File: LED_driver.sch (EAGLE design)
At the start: 15 parts

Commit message: Almost done with version 1 of the LED Driver Board
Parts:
- removed C4: 4.7uF 80V, resistor:C-EUC1210
- removed C6: 10uF, resistor:C-EUC0603
- removed U$11: VREG-ZXTR2105, BlueRobotics-Main:VREG-ZXTR2105
- removed U$3: 10uH, BlueRobotics-Main:INDUCTOR8040
- added C8: 47uF, PowerComponents:C-TANTALUM(10UF_150UF)
- added J1: (no value), SparkFun-Connectors:CONN_01
- added J8, J9: (no value), SparkFun-Connectors:CONN_021X02_NO_SILK
- added U$4: 15uH, DiscreteComponents:HCMA1305
- C3: value 47uF 63V -> 4.7uF; device SparkFun-Capacitors:CAP_POLPTH1 -> rcl:C-EUC0603
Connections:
- removed net VCC: C6.1, U$11.VOUT
- net GND: now also C3.2, C8.-, J8.1, J8.2; no longer C3.-, C4.2, C6.2, U$11.GND
- net LED+: now also U$4.2; no longer U$3.2
- net LED-PWM: now also J1.1
- net N$5: now also U$4.1; no longer U$3.1
- net VIN: now also C3.1, C8.+, J9.1, J9.2; no longer C3.+, C4.1, U$11.VIN
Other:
- note added: "399-3797-1-ND"

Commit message: Grant's design with the cheaper LED placed on the board
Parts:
- removed U$2: LED-MK-R, BlueRobotics-Main:LED-MK-R
- added U$3: LED_00H53, LED_00H53:LED_00H53
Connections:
- removed net EXT: U$2.THERMAL
- removed net LED+ISO: U$2.A
- removed net LED-ISO: U$2.C
- net LED+: now also U$3.LED+
- net LED-: now also U$3.LED-
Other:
- note removed: "MKRAWT-00-0000-0B00H4051"
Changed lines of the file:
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@@
 <parts>
 <part name="U$1" library="BlueRobotics-Main" deviceset="A6211" device=""/>
-<part name="U$2" library="BlueRobotics-Main" deviceset="LED-MK-R" device=""/>
 <part name="D1" library="BlueRobotics-Main" deviceset="DIODE-SCHOTTKY" device="SMA" value="60V 3A"/>
 <part name="R1" library="resistor" deviceset="R-US_" device="R2512" value="0.082 1W"/>
@@
 <part name="J8" library="SparkFun-Connectors" library_urn="urn:adsk.eagle:library:513" deviceset="CONN_02" device="1X02_NO_SILK" package3d_urn="urn:adsk.eagle:package:38051/1"/>
 <part name="J9" library="SparkFun-Connectors" library_urn="urn:adsk.eagle:library:513" deviceset="CONN_02" device="1X02_NO_SILK" package3d_urn="urn:adsk.eagle:package:38051/1"/>
+<part name="U$3" library="LED_00H53" deviceset="LED_00H53" device=""/>
 </parts>
 <sheets>
@@
 <text x="190.5" y="142.24" size="1.778" layer="97">NR8040T100M</text>
 <text x="180.34" y="104.14" size="1.778" layer="97" rot="R90">B360A-13-F</text>
-<text x="226.06" y="101.6" size="1.27" layer="97" rot="R90">MKRAWT-00-0000-0B00H4051</text>
 <text x="168.402" y="107.442" size="1.778" layer="97" rot="R90">Snubber</text>
 <text x="60.96" y="101.6" size="1.778" layer="91" rot="R90">
@@
 <instances>
 <instance part="U$1" gate="G$1" x="129.54" y="111.76"/>
-<instance part="U$2" gate="G$1" x="236.22" y="106.68" rot="R90"/>
 <instance part="D1" gate="G$1" x="185.42" y="109.22" rot="R90"/>
 <instance part="R1" gate="G$1" x="205.74" y="78.74" rot="R90"/>
@@
 <instance part="J8" gate="G$1" x="71.12" y="81.28"/>
 <instance part="J9" gate="G$1" x="45.72" y="81.28"/>
+<instance part="U$3" gate="G$1" x="231.14" y="114.3" rot="R270"/>
 </instances>
 <busses>
@@
 <pinref part="C2" gate="G$1" pin="1"/>
 <wire x1="205.74" y1="132.08" x2="205.74" y2="111.76" width="0.1524" layer="91"/>
-<wire x1="205.74" y1="132.08" x2="215.9" y2="132.08" width="0.1524" layer="91"/>
 <label x="208.28" y="132.08" size="1.778" layer="95"/>
 <pinref part="U$4" gate="G$1" pin="2"/>
 <wire x1="203.2" y1="132.08" x2="205.74" y2="132.08" width="0.1524" layer="91"/>
 <junction x="205.74" y="132.08"/>
+<pinref part="U$3" gate="G$1" pin="LED+"/>
+<wire x1="205.74" y1="132.08" x2="231.14" y2="132.08" width="0.1524" layer="91"/>
+<wire x1="231.14" y1="132.08" x2="231.14" y2="121.92" width="0.1524" layer="91"/>
 </segment>
 </net>
@@
 <wire x1="205.74" y1="104.14" x2="205.74" y2="91.44" width="0.1524" layer="91"/>
 <wire x1="205.74" y1="91.44" x2="205.74" y2="83.82" width="0.1524" layer="91"/>
-<wire x1="205.74" y1="91.44" x2="215.9" y2="91.44" width="0.1524" layer="91"/>
 <junction x="205.74" y="91.44"/>
 <wire x1="205.74" y1="91.44" x2="121.92" y2="91.44" width="0.1524" layer="91"/>
@@
 <wire x1="121.92" y1="114.3" x2="124.46" y2="114.3" width="0.1524" layer="91"/>
 <label x="208.28" y="91.44" size="1.778" layer="95"/>
-</segment>
-</net>
-<net name="LED-ISO" class="0">
-<segment>
-<pinref part="U$2" gate="G$1" pin="C"/>
-<wire x1="236.22" y1="104.14" x2="236.22" y2="91.44" width="0.1524" layer="91"/>
-<wire x1="236.22" y1="91.44" x2="220.98" y2="91.44" width="0.1524" layer="91"/>
-<label x="220.98" y="91.44" size="1.778" layer="95"/>
-</segment>
-</net>
-<net name="LED+ISO" class="0">
-<segment>
-<pinref part="U$2" gate="G$1" pin="A"/>
-<wire x1="236.22" y1="111.76" x2="236.22" y2="132.08" width="0.1524" layer="91"/>
-<wire x1="236.22" y1="132.08" x2="220.98" y2="132.08" width="0.1524" layer="91"/>
-<label x="220.98" y="132.08" size="1.778" layer="95"/>
-</segment>
-</net>
-<net name="EXT" class="0">
-<segment>
-<pinref part="U$2" gate="G$1" pin="THERMAL"/>
-<wire x1="241.3" y1="109.22" x2="248.92" y2="109.22" width="0.1524" layer="91"/>
-<label x="243.84" y="109.22" size="1.778" layer="95"/>
-</segment>
-</net>
+<pinref part="U$3" gate="G$1" pin="LED-"/>
+<wire x1="231.14" y1="106.68" x2="231.14" y2="91.44" width="0.1524" layer="91"/>
+<wire x1="231.14" y1="91.44" x2="205.74" y2="91.44" width="0.1524" layer="91"/>
+</segment>
+</net>

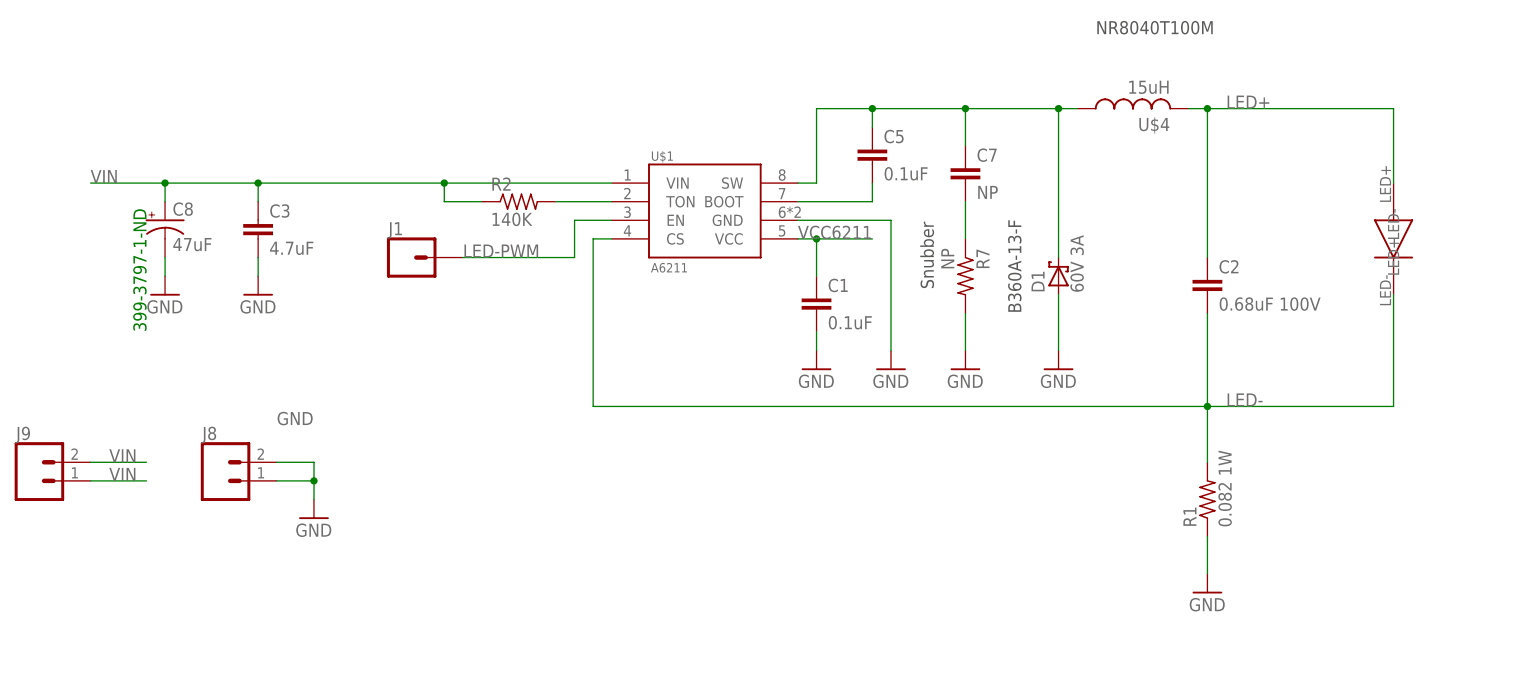
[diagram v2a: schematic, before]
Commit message: added nmos and connected EN to 12V
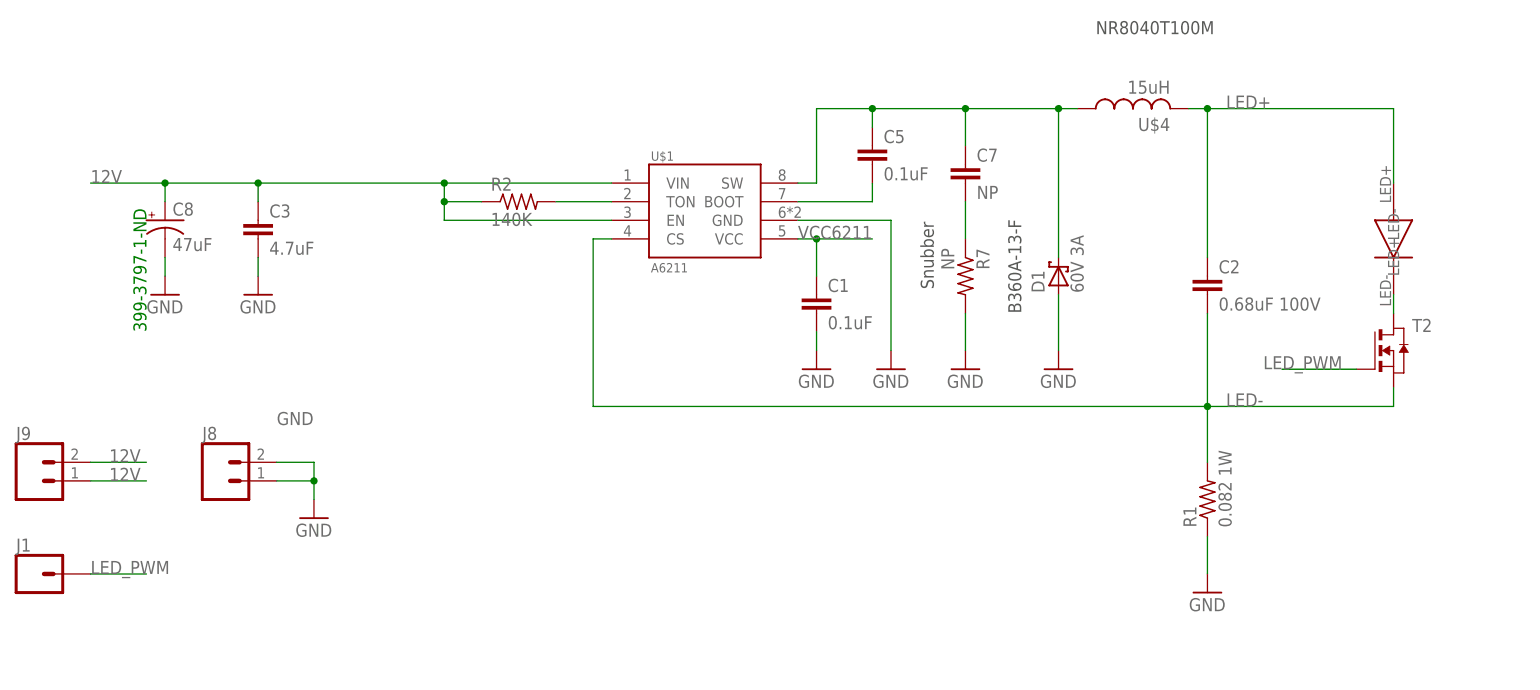
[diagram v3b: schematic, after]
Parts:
- added T2: (no value), zetex:NMOSSOT23
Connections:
- removed net LED-PWM: J1.1, U$1.EN
- removed net VIN: C3.1, C8.+, J9.1, J9.2, R2.1, U$1.VIN
- new net 12V: C3.1, C8.+, J9.1, J9.2, R2.1, U$1.EN, U$1.VIN
- new net LED_PWM: J1.1, T2.G
- new net N$3: T2.D, U$3.LED-
- net LED-: now also T2.S; no longer U$3.LED-
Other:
- moved on the sheet: J1
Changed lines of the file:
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@@
 <layers>
 <layer number="1" name="Top" color="4" fill="1" visible="no" active="no"/>
+<layer number="2" name="Route2" color="1" fill="3" visible="no" active="no"/>
+<layer number="3" name="Route3" color="4" fill="3" visible="no" active="no"/>
+<layer number="14" name="Route14" color="1" fill="6" visible="no" active="no"/>
+<layer number="15" name="Route15" color="4" fill="6" visible="no" active="no"/>
 <layer number="16" name="Bottom" color="1" fill="1" visible="no" active="no"/>
 <layer number="17" name="Pads" color="2" fill="1" visible="no" active="no"/>
@@
 <part name="J9" library="SparkFun-Connectors" library_urn="urn:adsk.eagle:library:513" deviceset="CONN_02" device="1X02_NO_SILK" package3d_urn="urn:adsk.eagle:package:38051/1"/>
 <part name="U$3" library="LED_00H53" deviceset="LED_00H53" device=""/>
+<part name="T2" library="zetex" deviceset="NMOSSOT23" device=""/>
 </parts>
 <sheets>
@@
 <attribute name="VALUE" x="64.516" y="112.649" size="1.778" layer="96"/>
 </instance>
-<instance part="J1" gate="G$1" x="96.52" y="111.76"/>
+<instance part="J1" gate="G$1" x="45.72" y="68.58"/>
 <instance part="C3" gate="G$1" x="76.2" y="116.84"/>
 <instance part="GND4" gate="1" x="83.82" y="76.2"/>
@@
 <instance part="J9" gate="G$1" x="45.72" y="81.28"/>
 <instance part="U$3" gate="G$1" x="231.14" y="114.3" rot="R270"/>
+<instance part="T2" gate="A" x="231.14" y="99.06"/>
 </instances>
 <busses>
@@
 </segment>
 </net>
-<net name="VIN" class="0">
+<net name="12V" class="0">
 <segment>
 <pinref part="U$1" gate="G$1" pin="VIN"/>
@@
 <junction x="63.5" y="121.92"/>
 <pinref part="C3" gate="G$1" pin="1"/>
+<pinref part="U$1" gate="G$1" pin="EN"/>
+<wire x1="124.46" y1="116.84" x2="101.6" y2="116.84" width="0.1524" layer="91"/>
+<wire x1="101.6" y1="119.38" x2="101.6" y2="116.84" width="0.1524" layer="91"/>
+<junction x="101.6" y="119.38"/>
 </segment>
 <segment>
@@
 <label x="55.88" y="81.28" size="1.778" layer="95"/>
 <pinref part="J9" gate="G$1" pin="1"/>
-</segment>
-</net>
-<net name="LED-PWM" class="0">
-<segment>
-<pinref part="U$1" gate="G$1" pin="EN"/>
-<wire x1="124.46" y1="116.84" x2="119.38" y2="116.84" width="0.1524" layer="91"/>
-<wire x1="119.38" y1="116.84" x2="119.38" y2="111.76" width="0.1524" layer="91"/>
-<wire x1="119.38" y1="111.76" x2="104.14" y2="111.76" width="0.1524" layer="91"/>
-<label x="104.14" y="111.76" size="1.778" layer="95"/>
-<pinref part="J1" gate="G$1" pin="1"/>
 </segment>
 </net>
@@
 <wire x1="121.92" y1="114.3" x2="124.46" y2="114.3" width="0.1524" layer="91"/>
 <label x="208.28" y="91.44" size="1.778" layer="95"/>
-<pinref part="U$3" gate="G$1" pin="LED-"/>
-<wire x1="231.14" y1="106.68" x2="231.14" y2="91.44" width="0.1524" layer="91"/>
 <wire x1="231.14" y1="91.44" x2="205.74" y2="91.44" width="0.1524" layer="91"/>
+<pinref part="T2" gate="A" pin="S"/>
+<wire x1="231.14" y1="93.98" x2="231.14" y2="91.44" width="0.1524" layer="91"/>
 </segment>
 </net>
@@
 </segment>
 </net>
+<net name="LED_PWM" class="0">
+<segment>
+<pinref part="J1" gate="G$1" pin="1"/>
+<wire x1="53.34" y1="68.58" x2="60.96" y2="68.58" width="0.1524" layer="91"/>
+<label x="53.34" y="68.58" size="1.778" layer="95"/>
+</segment>
+<segment>
+<pinref part="T2" gate="A" pin="G"/>
+<wire x1="226.06" y1="96.52" x2="215.9" y2="96.52" width="0.1524" layer="91"/>
+<label x="213.36" y="96.52" size="1.778" layer="95"/>
+</segment>
+</net>
+<net name="N$3" class="0">
+<segment>
+<pinref part="T2" gate="A" pin="D"/>
+<pinref part="U$3" gate="G$1" pin="LED-"/>
+<wire x1="231.14" y1="104.14" x2="231.14" y2="106.68" width="0.1524" layer="91"/>
+</segment>
+</net>
